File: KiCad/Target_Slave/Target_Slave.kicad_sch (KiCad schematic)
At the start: 30 parts, among them J1 ICSP, J2 LED, J3 I2C, J4 I2C, U1 PIC16F1788-IP, U2 TSSP4038

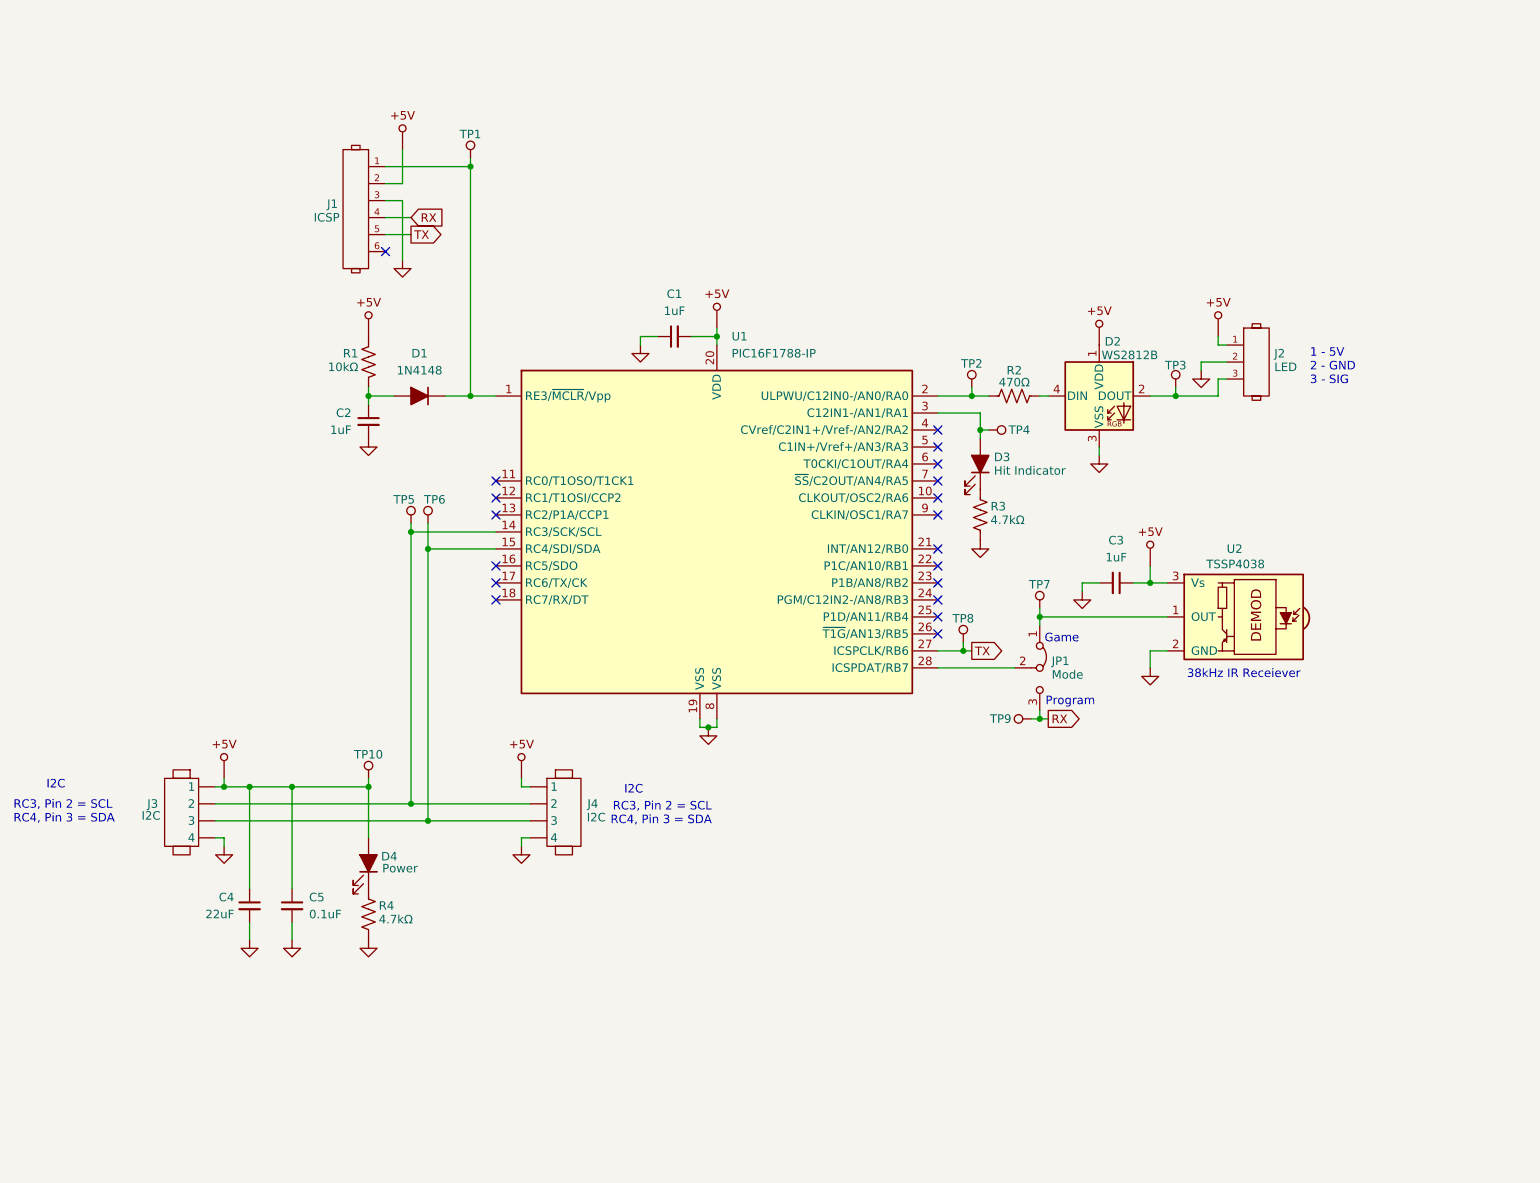
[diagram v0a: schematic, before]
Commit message: Add servo and stepper outputs to slave schematic and increase number of power pins at I2C headers
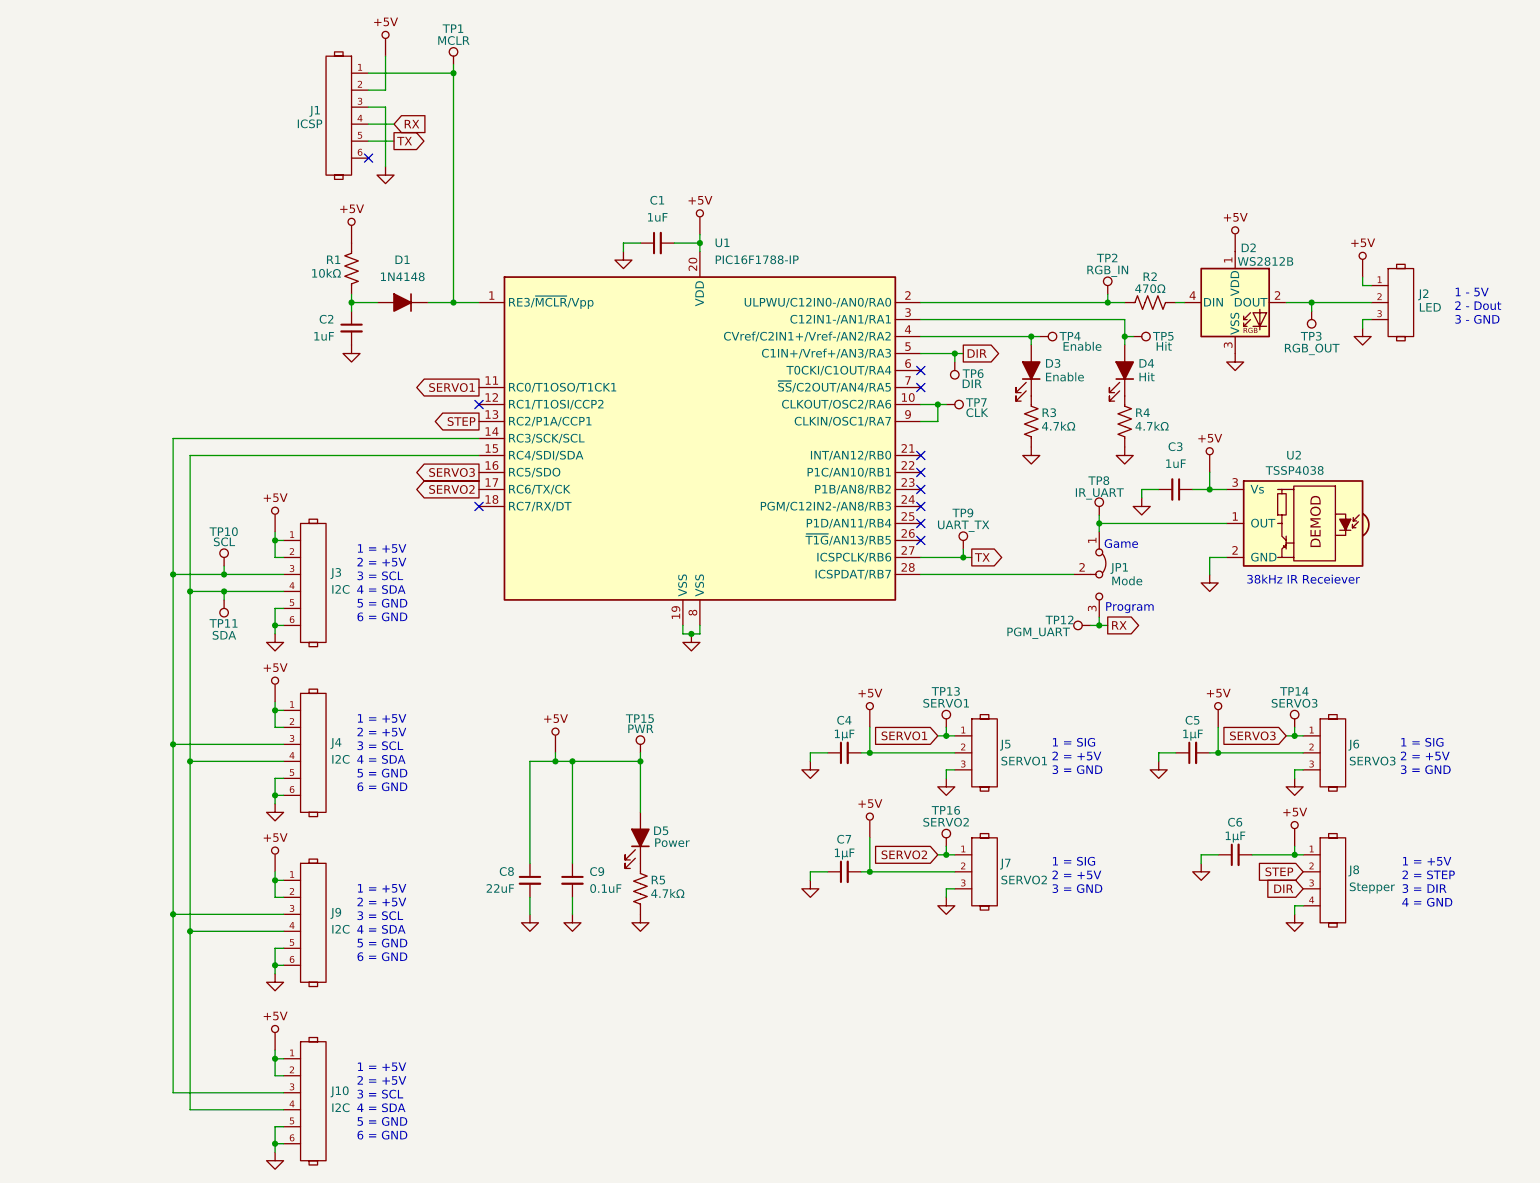
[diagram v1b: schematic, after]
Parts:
- removed J3, J4: I2C, 0_AKeller_Footprints:1x4_100mil_Header, symbol Libraries:Header_1x4
- added C4, C5, C6, C7: 1µF, Capacitor_SMD:C_0805_2012Metric_Pad1.18x1.45mm_HandSolder, symbol Device:C_Small
- added D3: Enable, LED_SMD:LED_0805_2012Metric_Pad1.15x1.40mm_HandSolder, symbol Device:LED_Filled
- added J10, J3, J4, J9: I2C, symbol 0_AKeller_Parts:Header_1x6
- added J5: SERVO1, symbol 0_AKeller_Parts:Header_1x3
- added J6: SERVO3, symbol 0_AKeller_Parts:Header_1x3
- added J7: SERVO2, symbol 0_AKeller_Parts:Header_1x3
- added J8: Stepper, symbol 0_AKeller_Parts:Header_1x4
- added R3: 4.7kΩ, symbol Device:R_US
- added TP13: SERVO1, 0_AKeller_Footprints:1x1_100mil_Header, symbol 0_AKeller_Parts:Test_Point
- added TP14: SERVO3, 0_AKeller_Footprints:1x1_100mil_Header, symbol 0_AKeller_Parts:Test_Point
- added TP16: SERVO2, 0_AKeller_Footprints:1x1_100mil_Header, symbol 0_AKeller_Parts:Test_Point
- added TP4: Enable, 0_AKeller_Footprints:1x1_100mil_Header, symbol 0_AKeller_Parts:Test_Point
- added TP6: DIR, 0_AKeller_Footprints:1x1_100mil_Header, symbol 0_AKeller_Parts:Test_Point
- added TP7: CLK, 0_AKeller_Footprints:1x1_100mil_Header, symbol 0_AKeller_Parts:Test_Point
- D4: renamed from D3; value Hit Indicator -> Hit
- TP1: value ~ -> MCLR
- TP10: renamed from TP5; value ~ -> SCL
- TP11: renamed from TP6; value ~ -> SDA
- TP12: renamed from TP9; value ~ -> PGM_UART
- TP15: renamed from TP10; value ~ -> PWR
- TP2: value ~ -> RGB_IN
- TP3: value ~ -> RGB_OUT
- TP5: renamed from TP4; value ~ -> Hit
- TP8: renamed from TP7; value ~ -> IR_UART
- TP9: renamed from TP8; value ~ -> UART_TX
- renumbered C4 to C8, C5 to C9, D4 to D5, R3 to R4, R4 to R5
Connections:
- net +5V: now also C4.2, C5.2, C6.2, C7.2, J10.1, J10.2, J3.1, J3.2, J4.1, J4.2, J5.2, J6.2, J7.2, J8.1, J9.1, J9.2
- net GND: now also J2.3, C4.1, C5.1, C6.1, C7.1, J10.5, J10.6, J3.5, J3.6, J4.5, J4.6, J5.3, J6.3, J7.3, J8.4, J9.5, J9.6, R3.2; no longer J2.2
- net at U1.10 (CLKOUT/OSC2/RA6): now also U1.9 (CLKIN/OSC1/RA7), TP7.1
- net SERVO1: now reaches U1.11 (RC0/T1OSO/T1CK1)
- net SERVO1: now also J5.1, TP13.1
- net STEP: now reaches U1.13 (RC2/P1A/CCP1)
- net STEP: now also J8.2
- net at TP10.1, U1.14 (RC3/SCK/SCL): now also J10.3, J3.3, J4.3, J9.3
- net at TP11.1, U1.15 (RC4/SDI/SDA): now also J10.4, J3.4, J4.4, J9.4
- net SERVO3: now reaches U1.16 (RC5/SDO)
- net SERVO3: now also J6.1, TP14.1
- net SERVO2: now reaches U1.17 (RC6/TX/CK)
- net SERVO2: now also J7.1, TP16.1
- net at U1.4 (CVref/C2IN1+/Vref-/AN2/RA2): now also D3.2 (A), TP4.1
- net DIR: now reaches U1.5 (C1IN+/Vref+/AN3/RA3)
- net DIR: now also J8.3, TP6.1
- net at D2.2 (DOUT), TP3.1: now also J2.2; no longer J2.3
- new net: D3.1 (K), R3.1
- no-connect marks 19 -> 11
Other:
- note added: "1 - 5V 2 - Dout 3 - GND"
- note added: "1 = +5V 2 = +5V 3 = SCL 4 = SDA 5 = GND 6 = GND"
- note added: "1 = +5V 2 = STEP 3 = DIR 4 = GND"
- note added: "1 = SIG 2 = +5V 3 = GND"
- note removed: "1 - 5V 2 - GND 3 - SIG"
- note removed: "I2C"
- note removed: "RC3, Pin 2 = SCL RC4, Pin 3 = SDA"
- moved on the sheet: C1, C2, C3, C8, C9, D1, D2, D4, D5, J1, J2, JP1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
